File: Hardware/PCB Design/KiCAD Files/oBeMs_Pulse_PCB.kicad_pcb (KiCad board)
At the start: 2 copper layers, 180.3 x 120.7 mm, 126 parts, among them P1 1WIRE_OUT, P10 5V, P11 3V3, P12 GND, P13 ADC_0-7, P14 ADC_8-15, P15 ADC_VREF_2, P16 ADC_VREF_1, P17 SPI_ADC_DAC, P18 DIO_OUTPUT, P19 PULL_UP, P2 1WIRE_SENSOR, P20 PULL_DOWN, P21 DIO_INPUT, P22 DIO_OUTPUT, P23 PULL_UP, P24 PULL_DOWN, P25 DIO_INPUT, P26 DIO_OUTPUT, P27 PULL_UP, P28 PULL_DOWN, P29 DIO_INPUT, P3 HARD_WDT, P34 DAC_A, P35 DAC_B, P36 PROTOTYPING_AREA, P4 LED 5-8, P6 AC_INPUT, P7 LED 1-4, Q1 BC546, Q2 BC556, U1 LM2575, U2 DS18B20, U3 TLC555, U4 4017, U5 MCP3008, U6 MCP3008, U7 MCP4802

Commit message: Update PCB
With notes from John
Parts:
- D7: footprint REInnovationFootprint:LED-5MM_larg_pad -> LED-5MM_larg_pad
- L1: footprint matts_components:C2V8_large_pads -> REInnovationFootprint:TH_Inductor
- moved RV1 35.8 mm to (81.3, 88.3), turned to 180 degrees
- moved P16 24.2 mm to (76.2, 99.1), turned to 90 degrees
- moved P15 23.9 mm to (76.2, 127.0), turned to 90 degrees
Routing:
- net +3.3V: track 642.2 -> 715.8 mm
- net Net-(R8-Pad1): track 12.9 -> 54.0 mm
- net Net-(P16-Pad2): track 4.44 -> 22.8 mm
- net Net-(P15-Pad2): track 4.44 -> 19.4 mm
- net Net-(P14-Pad1): track 43.8 -> 42.4 mm
- net Net-(P13-Pad1): track 44.0 -> 45.0 mm
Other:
- board text added: "GROUND"
- board text added: "VREF 1"
- board text added: "VREF 2"
- board text added: "oBeMS"
- board text removed: "ADC VREF 1"
- board text removed: "ADC VREF 2"
- board text removed: "PULL DOWN"
- board text removed: "oBeMs"

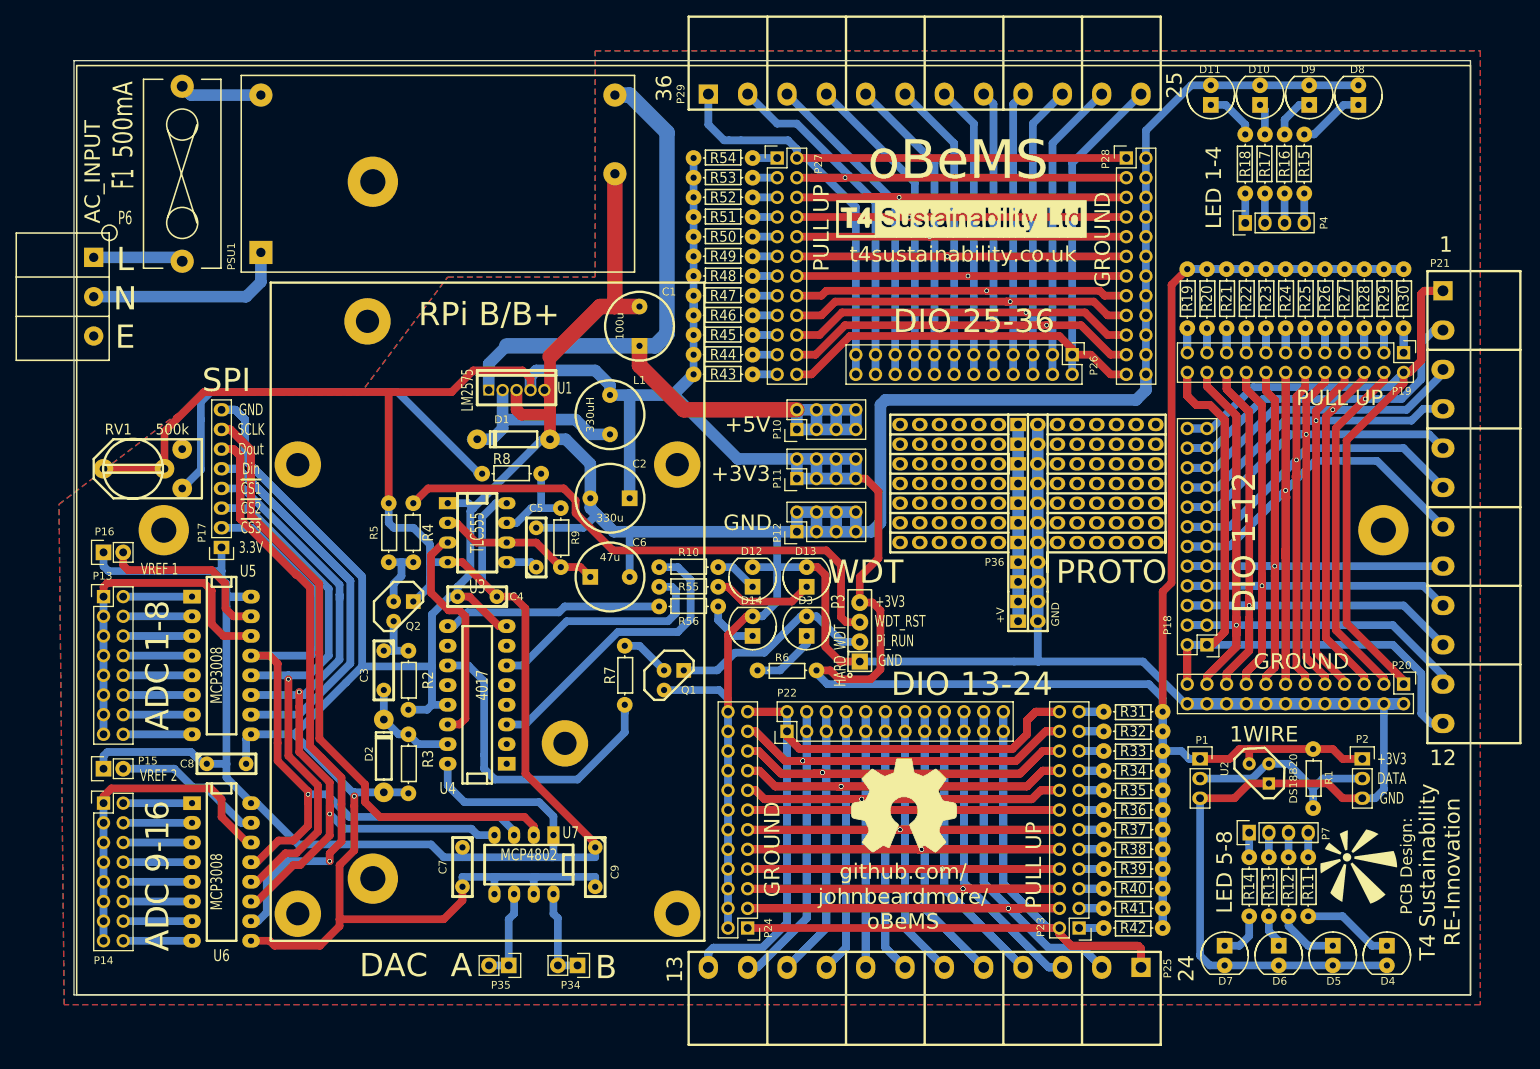
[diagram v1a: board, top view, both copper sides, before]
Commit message: Version 3 revision
Added 3A switching 5V supply and Capacitors axial and radial
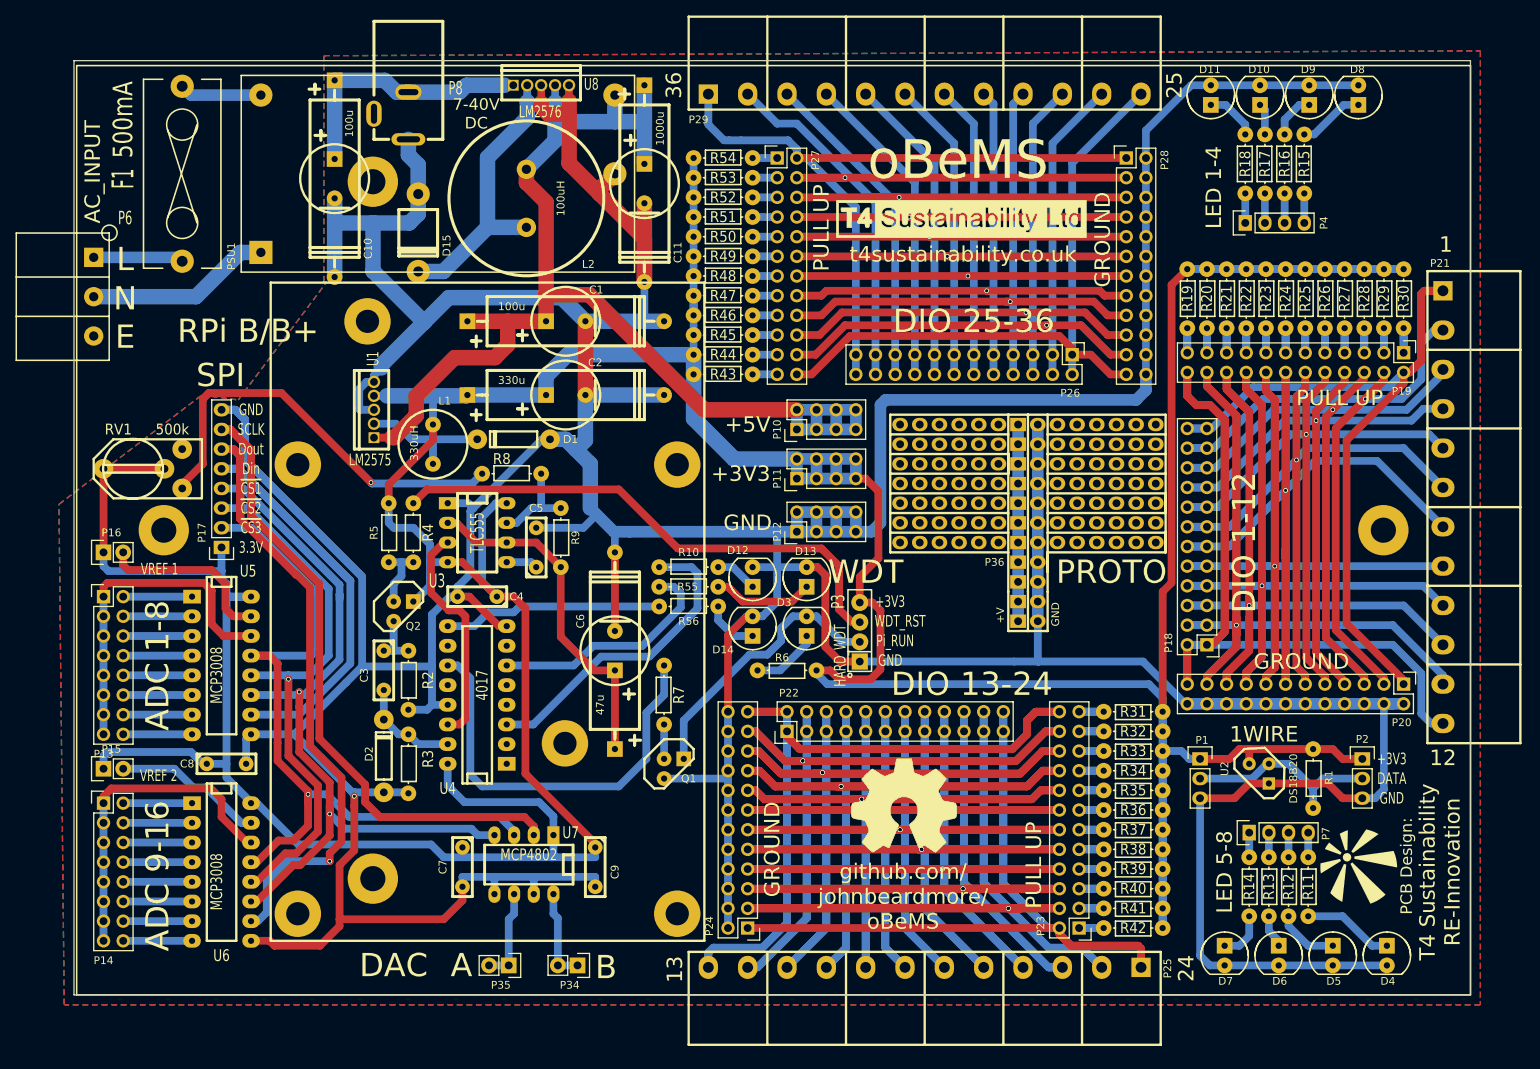
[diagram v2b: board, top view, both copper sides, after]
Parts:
- added C10: 100u, REInnovationFootprint:C2V8_VandA, F.Cu at (106.0, 50.8)
- added C11: 1000u, REInnovationFootprint:C2V8_VandA, F.Cu at (146.1, 51.4)
- added D15: 1N5822, REInnovationFootprint:TH_Diode_DO-201AD, F.Cu at (116.8, 57.8)
- added L2: 100uH, TH_Inductor_ELC18B101L, F.Cu at (130.8, 53.3)
- added P8: VIN_DC, REInnovationFootprint:DC_Power_2_1, F.Cu at (115.6, 45.7)
- added U8: LM2576, REInnovationFootprint:TO220_5PIN, F.Cu at (132.7, 38.7)
- C1, C2, C6: footprint matts_components:C2V8_large_pads -> REInnovationFootprint:C2V8_VandA
- D7: footprint LED-5MM_larg_pad -> REInnovationFootprint:LED-5MM_larg_pad
- LG2: footprint Logo:T4_32mm -> PCB_logo:T4_32mm
- LG3: footprint T4Logo:OSHW_13mm -> PCB_logo:OSHW_13mm
- P10, P11, P12: footprint Pin_Headers:Pin_Header_Straight_2x04 -> REInnovationFootprint:Pin_Header_Straight_2x04
- P13, P14: footprint Pin_Headers:Pin_Header_Straight_2x08 -> REInnovationFootprint:Pin_Header_Straight_2x08
- P15, P16, P34, P35: footprint Pin_Headers:Pin_Header_Straight_1x02 -> REInnovationFootprint:Pin_Header_Straight_1x02
- P17: footprint Pin_Headers:Pin_Header_Straight_1x08 -> REInnovationFootprint:Pin_Header_Straight_1x08
- P18, P19, P20, P22, P23, P24, P26, P27, P28: footprint Pin_Headers:Pin_Header_Straight_2x12 -> REInnovationFootprint:Pin_Header_Straight_2x12
- moved L1 23.2 mm to (118.7, 85.1)
- moved U1 18.6 mm to (111.1, 80.6), turned to 180 degrees
- moved C2 14.5 mm to (135.9, 78.7), turned to 0 degrees
- moved Q1 11.4 mm to (149.9, 127.0)
- moved C6 9.55 mm to (142.2, 111.8), turned to 90 degrees
- moved C1 9.55 mm to (135.9, 69.2), turned to 0 degrees
- moved R7 5.68 mm to (148.6, 117.5), turned to 90 degrees
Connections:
- P6 pad 3: (no net) -> GNDPWR
- PCB1 pad 1: (no net) -> Net-(PCB1-Pad1)
- RV1 pad 3: (no net) -> Net-(RV1-Pad3)
- U4 pad 1: (no net) -> Net-(U4-Pad1)
- U4 pad 10: (no net) -> Net-(U4-Pad10)
- U4 pad 12: (no net) -> Net-(U4-Pad12)
- U4 pad 2: (no net) -> Net-(U4-Pad2)
- U4 pad 4: (no net) -> Net-(U4-Pad4)
- U4 pad 5: (no net) -> Net-(U4-Pad5)
- U4 pad 7: (no net) -> Net-(U4-Pad7)
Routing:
- net GND: track 859.7 -> 1033.7 mm
- net /PowerSupply/VDC_IN+: track 0.00 -> 52.3 mm
- net Net-(D15-Pad2): track 0.00 -> 49.9 mm
- net +5V: track 167.8 -> 193.4 mm
- net Net-(C6-Pad1): track 21.3 -> 44.9 mm
- net Net-(R7-Pad2): track 41.7 -> 53.9 mm
- net /Watch Dog Timer/WDT_OUT: track 27.0 -> 36.4 mm
- net /PowerSupply/N: track 32.7 -> 24.0 mm
- net Net-(D1-Pad2): track 24.7 -> 17.9 mm
- net +3.3V: track 715.8 -> 709.6 mm
- net Net-(Q1-Pad2): track 6.40 -> 4.45 mm
- net /Watch Dog Timer/WDT_IN: track 70.5 -> 68.8 mm
- net Net-(R10-Pad1): track 39.2 -> 40.7 mm
- net Net-(R8-Pad1): track 54.0 -> 55.4 mm, vias 0 -> 1
- net Net-(R56-Pad1): track 28.4 -> 29.1 mm
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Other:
- net class Default: trace_width 1 -> 2
- board text added: "7-40V DC"

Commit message: Updated small changes.
Info and changes from email 18/12/15.
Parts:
- added H1: Bolt Hole, REInnovationFootprint:3mm_hole, F.Cu at (83.2, 76.8)
- added H2: Bolt Hole, REInnovationFootprint:3mm_hole, F.Cu at (77.5, 40.6)
- L2: footprint TH_Inductor_ELC18B101L -> REInnovationFootprint:TH_Inductor_ELC18B101L
- P8: value VIN_DC -> VDC_IN; footprint REInnovationFootprint:DC_Power_2_1 -> REInnovationFootprint:TH_CONN_2W
- moved P8 4.62 mm to (114.3, 41.3)
- moved PSU1 1.91 mm to (117.5, 50.2)
- moved F1 0.64 mm to (85.7, 50.2)
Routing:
- net GND: track 1033.7 -> 1012.9 mm
- net /PowerSupply/VDC_IN+: track 52.3 -> 48.2 mm
- net /PowerSupply/N: track 24.0 -> 22.1 mm
- net Net-(F1-Pad2): track 10.6 -> 9.36 mm
- net +5V: track 193.4 -> 193.9 mm

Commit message: Small changes on PCB
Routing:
- net Net-(D1-Pad2): track 17.9 -> 32.3 mm
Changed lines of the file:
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@@
     (thickness 1.6)
     (drawings 60)
-    (tracks 1615)
+    (tracks 1622)
     (zones 0)
     (modules 134)
@@
     (tags "LED led 5mm 5MM 100mil 2,54mm")
     (attr virtual)
-    (fp_text reference D11 (at 3.302 -0.127 180) (layer F.SilkS)
+    (fp_text reference D11 (at -3.175 -2.667 180) (layer F.SilkS)
       (effects (font (size 1 1) (thickness 0.15)))
     )
@@
     (tags "LED led 5mm 5MM 100mil 2,54mm")
     (attr virtual)
-    (fp_text reference D10 (at 3.302 -0.127 180) (layer F.SilkS)
+    (fp_text reference D10 (at -3.175 -3.302 180) (layer F.SilkS)
       (effects (font (size 1 1) (thickness 0.15)))
     )
@@
     (tags "LED led 5mm 5MM 100mil 2,54mm")
     (attr virtual)
-    (fp_text reference D9 (at 3.302 -0.127 180) (layer F.SilkS)
+    (fp_text reference D9 (at -3.175 -3.302 180) (layer F.SilkS)
       (effects (font (size 1 1) (thickness 0.15)))
     )
@@
     (tags "LED led 5mm 5MM 100mil 2,54mm")
     (attr virtual)
-    (fp_text reference D8 (at 3.302 -0.127 180) (layer F.SilkS)
+    (fp_text reference D8 (at -3.175 -3.302 180) (layer F.SilkS)
       (effects (font (size 1 1) (thickness 0.15)))
     )
@@
     (effects (font (size 2 2) (thickness 0.5)))
   )
-  (gr_text "PULL UP" (at 196.342 139.446 90) (layer F.SilkS)
+  (gr_text "PULL UP" (at 196.215 139.065 90) (layer F.SilkS)
     (effects (font (size 2 2) (thickness 0.5)))
   )
@@
     (effects (font (size 3 3) (thickness 0.75)))
   )
+  (segment (start 118.745 82.55) (end 118.745 78.845) (width 2) (layer B.Cu) (net 1))
   (segment (start 152.4 73.533) (end 152.4 81.788) (width 2) (layer B.Cu) (net 1))
   (segment (start 157.607 86.995) (end 165.735 86.995) (width 2) (layer B.Cu) (net 1))
@@
   (segment (start 152.4 81.026) (end 158.369 86.995) (width 1) (layer B.Cu) (net 1))
   (segment (start 158.369 86.995) (end 165.735 86.995) (width 1) (layer B.Cu) (net 1))
-  (segment (start 118.745 82.55) (end 118.745 78.845) (width 1) (layer B.Cu) (net 1))
   (segment (start 118.745 78.845) (end 119.126 78.845) (width 1) (layer B.Cu) (net 1))
   (segment (start 111.125 78.845) (end 112.776 78.845) (width 1) (layer B.Cu) (net 1))
@@
   (segment (start 124.333 97.79) (end 128.27 97.79) (width 1) (layer F.Cu) (net 22))
   (segment (start 121.793 95.25) (end 124.333 97.79) (width 1) (layer F.Cu) (net 22))
+  (segment (start 118.745 85.217) (end 118.745 87.63) (width 2) (layer B.Cu) (net 23))
+  (segment (start 112.649 82.445) (end 113.941 82.445) (width 2) (layer B.Cu) (net 23))
+  (segment (start 113.941 82.445) (end 115.951 84.455) (width 2) (layer B.Cu) (net 23))
+  (segment (start 115.951 84.455) (end 116.713 85.217) (width 2) (layer B.Cu) (net 23))
+  (segment (start 116.713 85.217) (end 118.745 85.217) (width 2) (layer B.Cu) (net 23))
+  (segment (start 118.745 85.217) (end 123.698 85.217) (width 2) (layer B.Cu) (net 23))
+  (segment (start 123.698 85.217) (end 124.46 84.455) (width 2) (layer B.Cu) (net 23))
   (segment (start 118.745 87.63) (end 118.745 84.455) (width 1) (layer B.Cu) (net 23))
-  (segment (start 111.125 82.445) (end 113.941 82.445) (width 1) (layer B.Cu) (net 23))
+  (segment (start 111.125 82.445) (end 112.649 82.445) (width 1) (layer B.Cu) (net 23))
   (segment (start 115.951 84.455) (end 118.745 84.455) (width 1) (layer B.Cu) (net 23))
   (segment (start 118.745 84.455) (end 124.46 84.455) (width 1) (layer B.Cu) (net 23))

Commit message: Updates from email 21/12/15
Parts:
- removed P35: DAC_B, REInnovationFootprint:Pin_Header_Straight_1x02
- removed R10, R55, R56: 120, REInnovationFootprint:TH_Resistor_1
- added D16: BRIDGE, REInnovationFootprint:TH_BridgeRect_8A, F.Cu at (103.5, 41.3)
- C2: value 330u -> 1000u
- C7, C8: value 100n -> 1000n
- D1: value IN5819 -> 1N5822; footprint REInnovationFootprint:TH_Diode_1 -> REInnovationFootprint:TH_Diode_DO-201AD
- P1: value 1WIRE_OUT -> 1WIRE; footprint Pin_Headers:Pin_Header_Straight_1x03 -> REInnovationFootprint:Pin_Header_Straight_1x04
- P10, P11, P12: footprint REInnovationFootprint:Pin_Header_Straight_2x04 -> REInnovationFootprint:Pin_Header_Straight_2x08
- P2: value 1WIRE_SENSOR -> EXT_CAP; footprint Pin_Headers:Pin_Header_Straight_1x03 -> matts_components:SIL-2_wide_lg_pad
- P20, P24, P28: value PULL_DOWN -> GROUND
- P34: value DAC_A -> DAC; footprint REInnovationFootprint:Pin_Header_Straight_1x02 -> REInnovationFootprint:Pin_Header_Straight_2x04
- P36: footprint REInnovationFootprint:PROTO_AREA -> PROTO_AREA
- R6: value 120 -> 100
- moved P2 143.3 mm to (124.5, 39.4), turned to 180 degrees
- moved C10 29.4 mm to (102.9, 80.0)
- moved R8 20.1 mm to (109.9, 95.2), turned to 270 degrees
- moved P12 9.54 mm to (156.2, 95.9)
- moved P10 9.53 mm to (156.2, 83.2)
- moved P11 9.53 mm to (156.2, 89.5)
- moved U2 6.35 mm to (231.1, 128.3)
- moved R1 5.08 mm to (237.5, 128.3)
- moved P8 3.81 mm to (110.5, 41.3)
- moved P34 3.07 mm to (134.6, 151.1)
- moved P1 2.01 mm to (218.4, 123.8)
- moved D1 1.42 mm to (130.2, 85.7)
- moved U8 0.63 mm to (133.3, 38.7)
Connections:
- C10 pad 1: /PowerSupply/VDC_IN+ -> Net-(C10-Pad1)
- P1 pad 3: GND -> /TemperatureSensor/D-1-Wire
- P2 pad 1: +3.3V -> Net-(C10-Pad1)
- P2 pad 2: /TemperatureSensor/D-1-Wire -> GND
- P34 pad 2: Net-(P34-Pad1) -> GND
- P36 pad 2: GND -> Net-(P36-Pad2)
- P6 pad 3: GNDPWR -> (no net)
- P8 pad 1: /PowerSupply/VDC_IN+ -> /PowerSupply/VIN_A
- P8 pad 2: GND -> /PowerSupply/VIN_B
- PCB1 pad 1: Net-(PCB1-Pad1) -> (no net)
- RV1 pad 3: Net-(RV1-Pad3) -> (no net)
- U4 pad 1: Net-(U4-Pad1) -> (no net)
- U4 pad 10: Net-(U4-Pad10) -> (no net)
- U4 pad 12: Net-(U4-Pad12) -> (no net)
- U4 pad 2: Net-(U4-Pad2) -> (no net)
- U4 pad 3: Net-(R10-Pad1) -> Net-(D12-Pad1)
- U4 pad 4: Net-(U4-Pad4) -> (no net)
- U4 pad 5: Net-(U4-Pad5) -> (no net)
- U4 pad 6: Net-(R55-Pad1) -> Net-(D13-Pad1)
- U4 pad 7: Net-(U4-Pad7) -> (no net)
- U4 pad 9: Net-(R56-Pad1) -> Net-(D14-Pad1)
- U7 pad 6: Net-(P35-Pad1) -> Net-(P34-Pad5)
- U8 pad 1: /PowerSupply/VDC_IN+ -> Net-(C10-Pad1)
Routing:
- net +5V: track 193.9 -> 436.6 mm, vias 0 -> 3
- net Net-(C10-Pad1): track 0.00 -> 156.6 mm
- net GND: track 1012.9 -> 1132.1 mm, vias 1 -> 6
- net Net-(D15-Pad2): track 49.9 -> 100.7 mm
- net /PowerSupply/VDC_IN+: track 48.2 -> 0.00 mm
- net Net-(R10-Pad1): track 40.7 -> 0.00 mm
- net Net-(D14-Pad1): track 7.06 -> 45.2 mm
- net Net-(D12-Pad1): track 5.50 -> 42.3 mm, vias 0 -> 1
- net Net-(D13-Pad1): track 13.0 -> 45.3 mm, vias 0 -> 1
- net Net-(R55-Pad1): track 30.5 -> 0.00 mm
- net Net-(R56-Pad1): track 29.1 -> 0.00 mm
- net Net-(P36-Pad2): track 0.00 -> 25.4 mm
- net Net-(R8-Pad2): track 13.0 -> 34.7 mm
- net /PowerSupply/VIN_A: track 0.00 -> 19.1 mm
- net Net-(P35-Pad1): track 12.0 -> 0.00 mm
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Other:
- board text added: "+"
- board text added: "VERSION: V0000 DATE: 21/12/15"

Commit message: More small changes 22/12/15
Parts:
- added P9: V?, matts_components:SIL-3_solder_connect, F.Cu at (203.8, 116.7)
- P36: footprint PROTO_AREA -> PROTO_AREA_16x14
- P8: value VDC_IN -> LT_PWR
- RV1: footprint matts_components:RV_various_lg_pad -> RV_various_lg_pad
- moved P36 11.0 mm to (181.0, 78.1)
- moved P3 2.67 mm to (171.3, 113.0)
- moved L2 2.54 mm to (130.8, 55.9)
- moved LG3 2.05 mm to (178.8, 133.6)
- moved P2 1.91 mm to (124.5, 41.3)
- moved D12 1.65 mm to (158.4, 102.2)
- moved D14 1.65 mm to (158.4, 108.6)
- moved R6 1.65 mm to (162.8, 114.3)
- moved D13 1.65 mm to (165.4, 102.2)
- moved D3 1.65 mm to (165.4, 108.6)
- moved C1 0.63 mm to (135.9, 69.8)
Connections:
- P36 pad 2: Net-(P36-Pad2) -> GND
- P6 pad 3: (no net) -> GNDPWR
- PCB1 pad 1: (no net) -> Net-(PCB1-Pad1)
- RV1 pad 3: (no net) -> Net-(RV1-Pad3)
- U4 pad 1: (no net) -> Net-(U4-Pad1)
- U4 pad 10: (no net) -> Net-(U4-Pad10)
- U4 pad 12: (no net) -> Net-(U4-Pad12)
- U4 pad 2: (no net) -> Net-(U4-Pad2)
- U4 pad 4: (no net) -> Net-(U4-Pad4)
- U4 pad 5: (no net) -> Net-(U4-Pad5)
- U4 pad 7: (no net) -> Net-(U4-Pad7)
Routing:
- net +5V: track 436.6 -> 526.3 mm, vias 3 -> 4
- net Net-(P36-Pad1): track 25.4 -> 93.3 mm
- net GND: track 1132.1 -> 1161.5 mm, vias 6 -> 8
- net Net-(P36-Pad2): track 25.4 -> 0.00 mm
- net +3.3V: track 720.6 -> 739.1 mm
- net Net-(C10-Pad1): track 156.6 -> 169.7 mm
- net Net-(D15-Pad2): track 100.7 -> 96.8 mm
- net /Watch Dog Timer/WDT_IN: track 70.6 -> 67.6 mm
- net Net-(D13-Pad1): track 45.3 -> 43.6 mm
- net Net-(D12-Pad1): track 42.3 -> 40.7 mm
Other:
- net class Default: trace_width 2 -> 1
- board text added: "3V3"
- board text added: "5V"
- board text added: "RPi / RPi 2"
- board text added: "RST"
- board text added: "RUN"
- board text removed: "Pi_RUN"
- board text removed: "RPi B/B+"
- board text removed: "WDT_RST"

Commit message: Rev 6. Final changes before PCB v0000 done
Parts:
- added P30: UNREG_DC, REInnovationFootprint:Pin_Header_Straight_2x03, F.Cu at (109.2, 56.5)
- added P31: V2?, REInnovationFootprint:SIL-3_solder_connect, F.Cu at (203.8, 116.8)
- H1, H2: value Bolt Hole -> AC Cover Mount Hole
- P36: footprint PROTO_AREA_16x14 -> REInnovationFootprint:PROTO_AREA_16x14
- P9: value V? -> V1?; footprint matts_components:SIL-3_solder_connect -> REInnovationFootprint:SIL-3_solder_connect
- PCB1: footprint REInnovationFootprint:PCB_120x150_WISKA -> PCB_120x150_WISKA
- RV1: footprint RV_various_lg_pad -> matts_components:RV_various_lg_pad
- moved P9 20.3 mm to (183.5, 116.8)
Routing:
- net Net-(P36-Pad1): track 93.3 -> 36.2 mm
- net GND: track 1161.5 -> 1117.1 mm, vias 8 -> 6
- net Net-(P31-Pad2): track 0.00 -> 36.2 mm
- net Net-(C10-Pad1): track 169.7 -> 196.0 mm
- net +5V: track 526.3 -> 530.8 mm, vias 4 -> 5
- net +3.3V: track 739.1 -> 742.2 mm, vias 0 -> 2
